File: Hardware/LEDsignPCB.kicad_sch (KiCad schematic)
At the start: 27 parts, among them J1 Conn_01x03, J2 Conn_01x03, J3 Conn_01x04, J4 Conn_01x04, J5 USB_C_Receptacle_USB2.0_14P, SW5 SW_Push, SW6 SW_Push, U12 ESP32-S3-WROOM-1

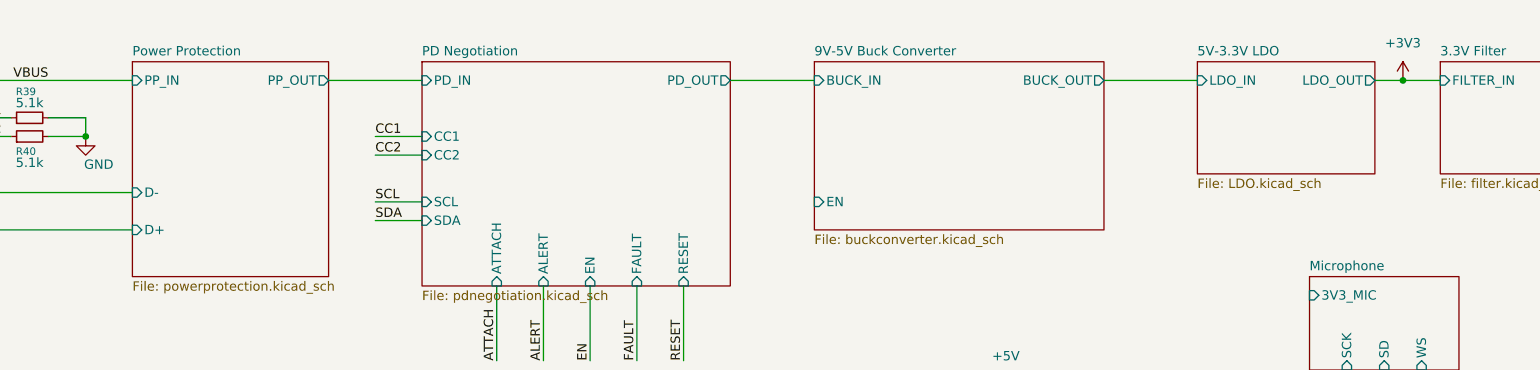
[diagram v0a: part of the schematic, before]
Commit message: reorganization into 4 sheets, schematic not finalized yet
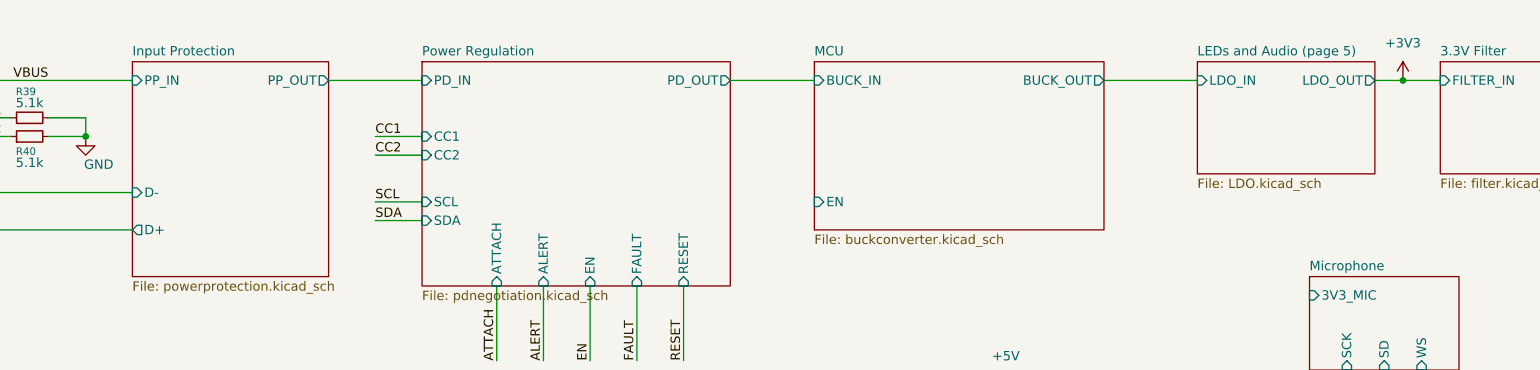
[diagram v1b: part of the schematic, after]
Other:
- sheet 5V-3.3V LDO renamed LEDs and Audio (page 5)
- sheet 9V-5V Buck Converter renamed MCU
- sheet PD Negotiation renamed Power Regulation
- sheet Power Protection renamed Input Protection
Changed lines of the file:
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@@
 			(color 0 0 0 0)
 		)
-		(property "Sheetname" "5V-3.3V LDO"
+		(property "Sheetname" "LEDs and Audio (page 5)"
 			(at 214.63 23.4184 0)
 			(show_name no)
@@
 			(color 0 0 0 0)
 		)
-		(property "Sheetname" "9V-5V Buck Converter"
+		(property "Sheetname" "MCU"
 			(at 162.56 23.4184 0)
 			(show_name no)
@@
 			(color 0 0 0 0)
 		)
-		(property "Sheetname" "Power Protection"
+		(property "Sheetname" "Input Protection"
 			(at 69.85 23.4184 0)
 			(show_name no)
@@
 			)
 		)
-		(pin "D+" input
+		(pin "D+" output
 			(at 69.85 46.99 180)
 			(effects
@@
 			(color 0 0 0 0)
 		)
-		(property "Sheetname" "PD Negotiation"
+		(property "Sheetname" "Power Regulation"
 			(at 109.22 23.4184 0)
 			(show_name no)

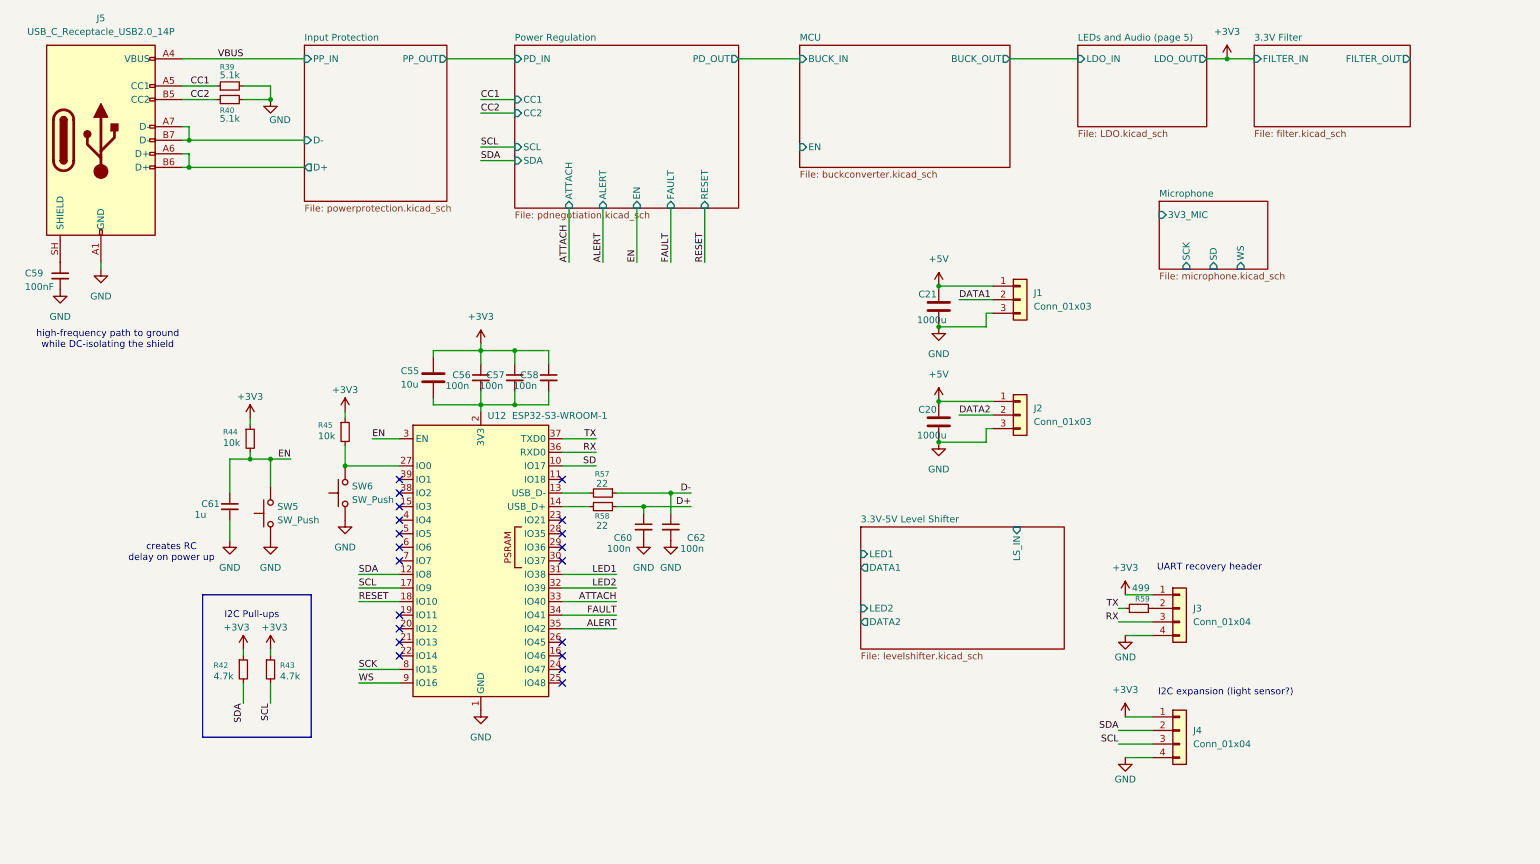
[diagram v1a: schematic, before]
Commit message: cleaned up schematic hierarchy
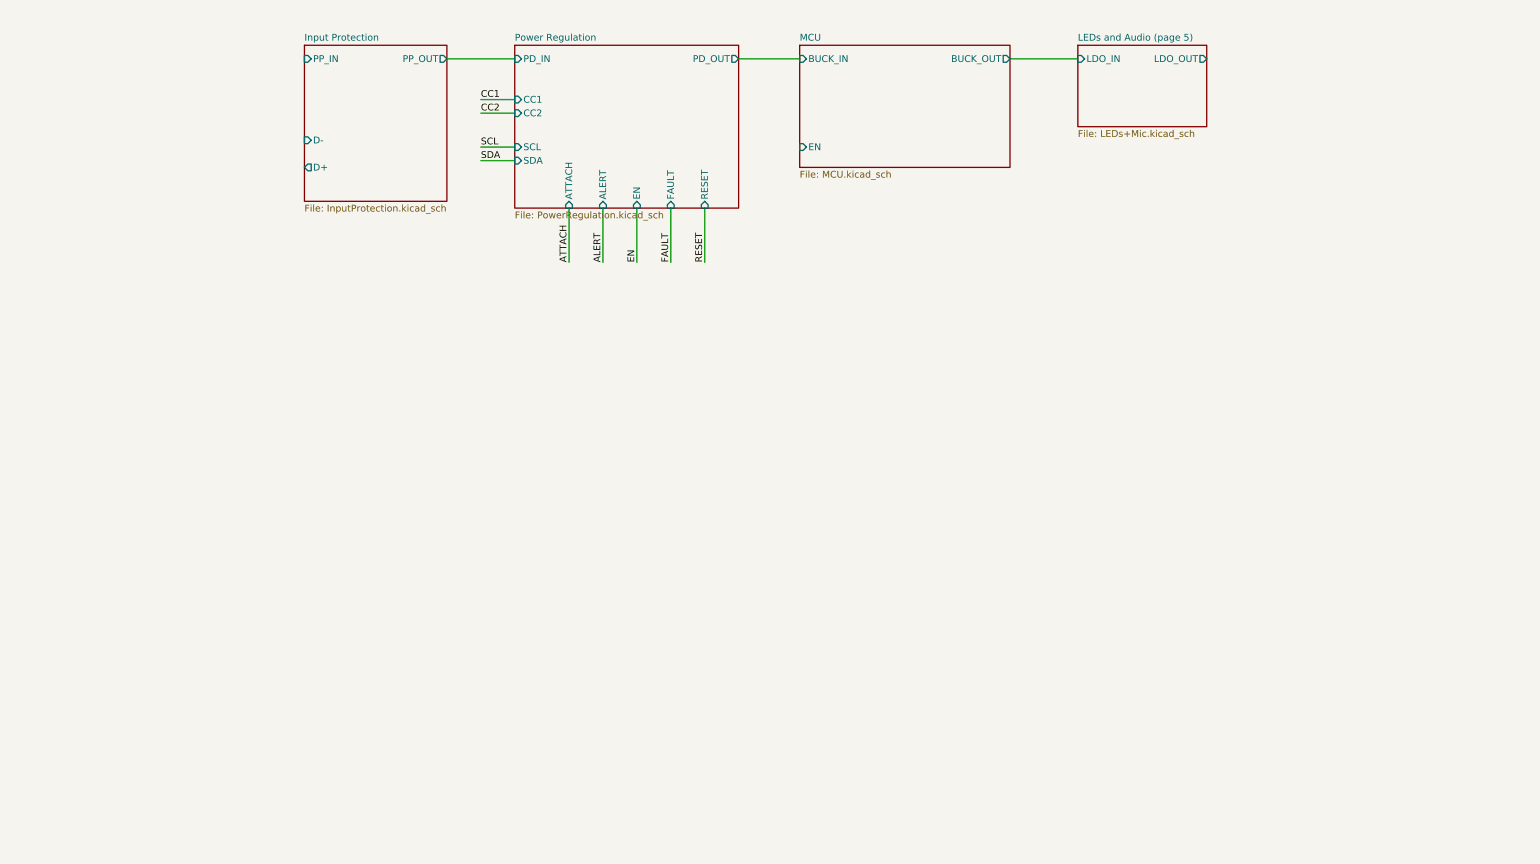
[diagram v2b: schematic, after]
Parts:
- removed C20, C21: 1000u, symbol Device:C
- removed C55: 10u, symbol Device:C
- removed C56, C57, C58, C60, C62: 100n, symbol Device:C_Small
- removed C59: 100nF, symbol Device:C_Small
- removed C61: 1u, symbol Device:C_Small
- removed J1, J2: Conn_01x03, symbol Connector_Generic:Conn_01x03
- removed J3, J4: Conn_01x04, symbol Connector_Generic:Conn_01x04
- removed J5: USB_C_Receptacle_USB2.0_14P, symbol Connector:USB_C_Receptacle_USB2.0_14P
- removed R39, R40: 5.1k, symbol Device:R_Small
- removed R42, R43: 4.7k, symbol Device:R_Small
- removed R44, R45: 10k, symbol Device:R_Small
- removed R57, R58: 22, symbol Device:R_Small
- removed R59: 499, symbol Device:R_Small
- removed SW5, SW6: SW_Push, symbol Switch:SW_Push
- removed U12: ESP32-S3-WROOM-1, RF_Module:ESP32-S3-WROOM-1, symbol RF_Module:ESP32-S3-WROOM-1
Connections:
- no-connect marks 20 -> 0
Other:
- removed sheet 3.3V Filter
- removed sheet 3.3V-5V Level Shifter
- removed sheet Microphone
- sheet Input Protection: file powerprotection.kicad_sch -> InputProtection.kicad_sch
- sheet LEDs and Audio (page 5): file LDO.kicad_sch -> LEDs+Mic.kicad_sch
- sheet MCU: file buckconverter.kicad_sch -> MCU.kicad_sch
- sheet Power Regulation: file pdnegotiation.kicad_sch -> PowerRegulation.kicad_sch
- note removed: "I2C Pull-ups"
- note removed: "I2C expansion (light sensor?)"
- note removed: "UART recovery header"
- note removed: "creates RC delay on power up"
- note removed: "high-frequency path to ground while DC-isolating the shield"

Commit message: new buck ic with 6A current limit, more organization and changes
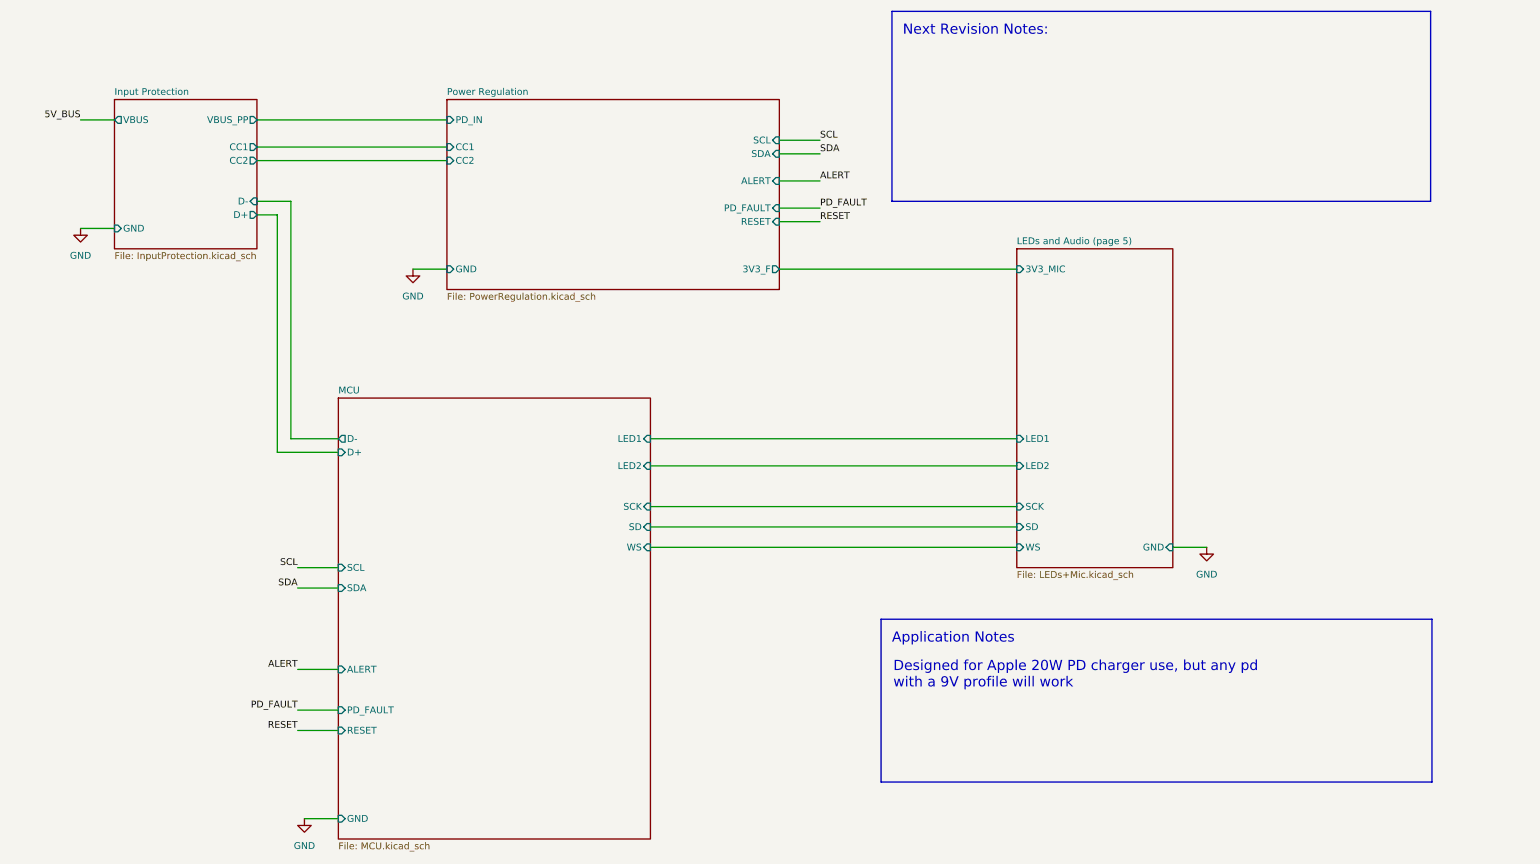
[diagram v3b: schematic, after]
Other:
- sheet Input Protection ports: added CC1, CC2, GND, VBUS, VBUS_PP; removed PP_IN, PP_OUT
- sheet LEDs and Audio (page 5) ports: added 3V3_MIC, GND, LED1, LED2, SCK, SD, WS; removed LDO_IN, LDO_OUT
- sheet MCU ports: added ALERT, D+, D-, GND, LED1, LED2, PD_FAULT, RESET, SCK, SCL, SD, SDA, WS; removed BUCK_IN, BUCK_OUT, EN
- sheet Power Regulation ports: added 3V3_F, GND, PD_FAULT; removed ATTACH, EN, FAULT, PD_OUT
- note added: "Application Notes"
- note added: "Designed for Apple 20W PD charger use, but any pd with a 9V profile will work"
- note added: "Next Revision Notes:"

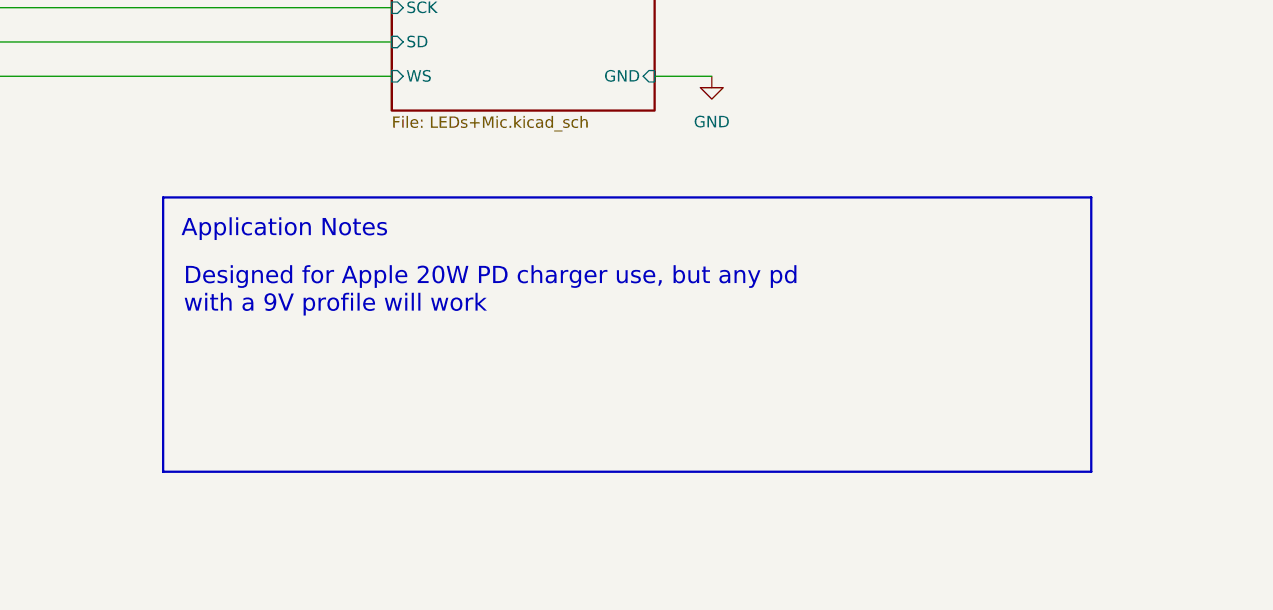
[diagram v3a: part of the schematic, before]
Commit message: added more testpoints and indicator LEDs, added application notes
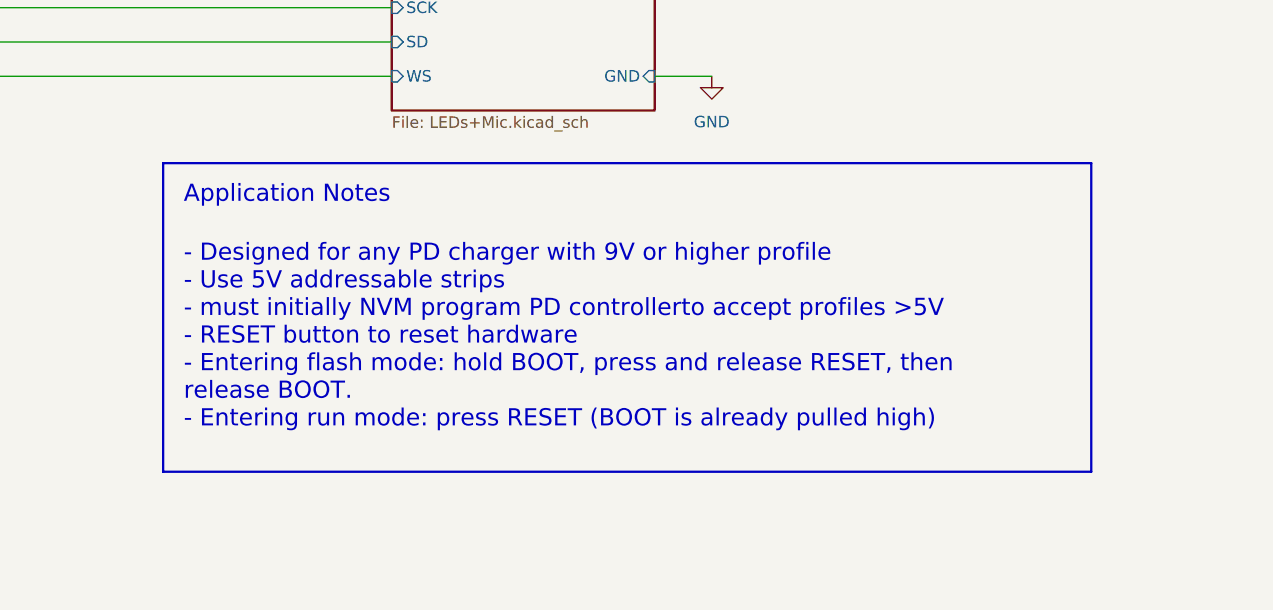
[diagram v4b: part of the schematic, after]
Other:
- note added: "- Designed for any PD charger with 9V or higher profile - Use 5V addressable strips - must initially NVM program PD controllerto accept profiles >5V - RESET button to reset hardware - Entering flash mode: hold BOOT, press and release RESET, then release BOOT. - Entering run mode: press RESET (BOOT is already pulled high)"
- note removed: "Designed for Apple 20W PD charger use, but any pd with a 9V profile will work"
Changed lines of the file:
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@@
 	(paper "A4")
 	(rectangle
-		(start 177.8 131.572)
+		(start 177.8 127.762)
 		(end 280.924 162.052)
 		(stroke
@@
 		)
 	)
-	(text "Designed for Apple 20W PD charger use, but any pd \nwith a 9V profile will work"
+	(text "- Designed for any PD charger with 9V or higher profile\n- Use 5V addressable strips\n- must initially NVM program PD controllerto accept profiles >5V\n- RESET button to reset hardware\n- Entering flash mode: hold BOOT, press and release RESET, then\nrelease BOOT.\n- Entering run mode: press RESET (BOOT is already pulled high)"
 		(exclude_from_sim no)
-		(at 180.086 141.986 0)
+		(at 180.086 147.066 0)
 		(effects
 			(font
@@
 	(text "Application Notes"
 		(exclude_from_sim no)
-		(at 179.832 135.128 0)
+		(at 180.086 131.318 0)
 		(effects
 			(font
